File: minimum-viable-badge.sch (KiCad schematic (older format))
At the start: 33 parts, among them J1 EDGE_CONNECTOR, P1 BATTERY, P11 MECH, P12 MECH, P13 MECH, P2 USB, P3 BUTTON_A, P4 BUTTON_B, P6 POT_LONG, P9 POT_SHORT, Q1 S8050, Q2 S8050, SW1 PRGM, SW2 RESET, U1 CP2102, U2 ESP32-WROOM

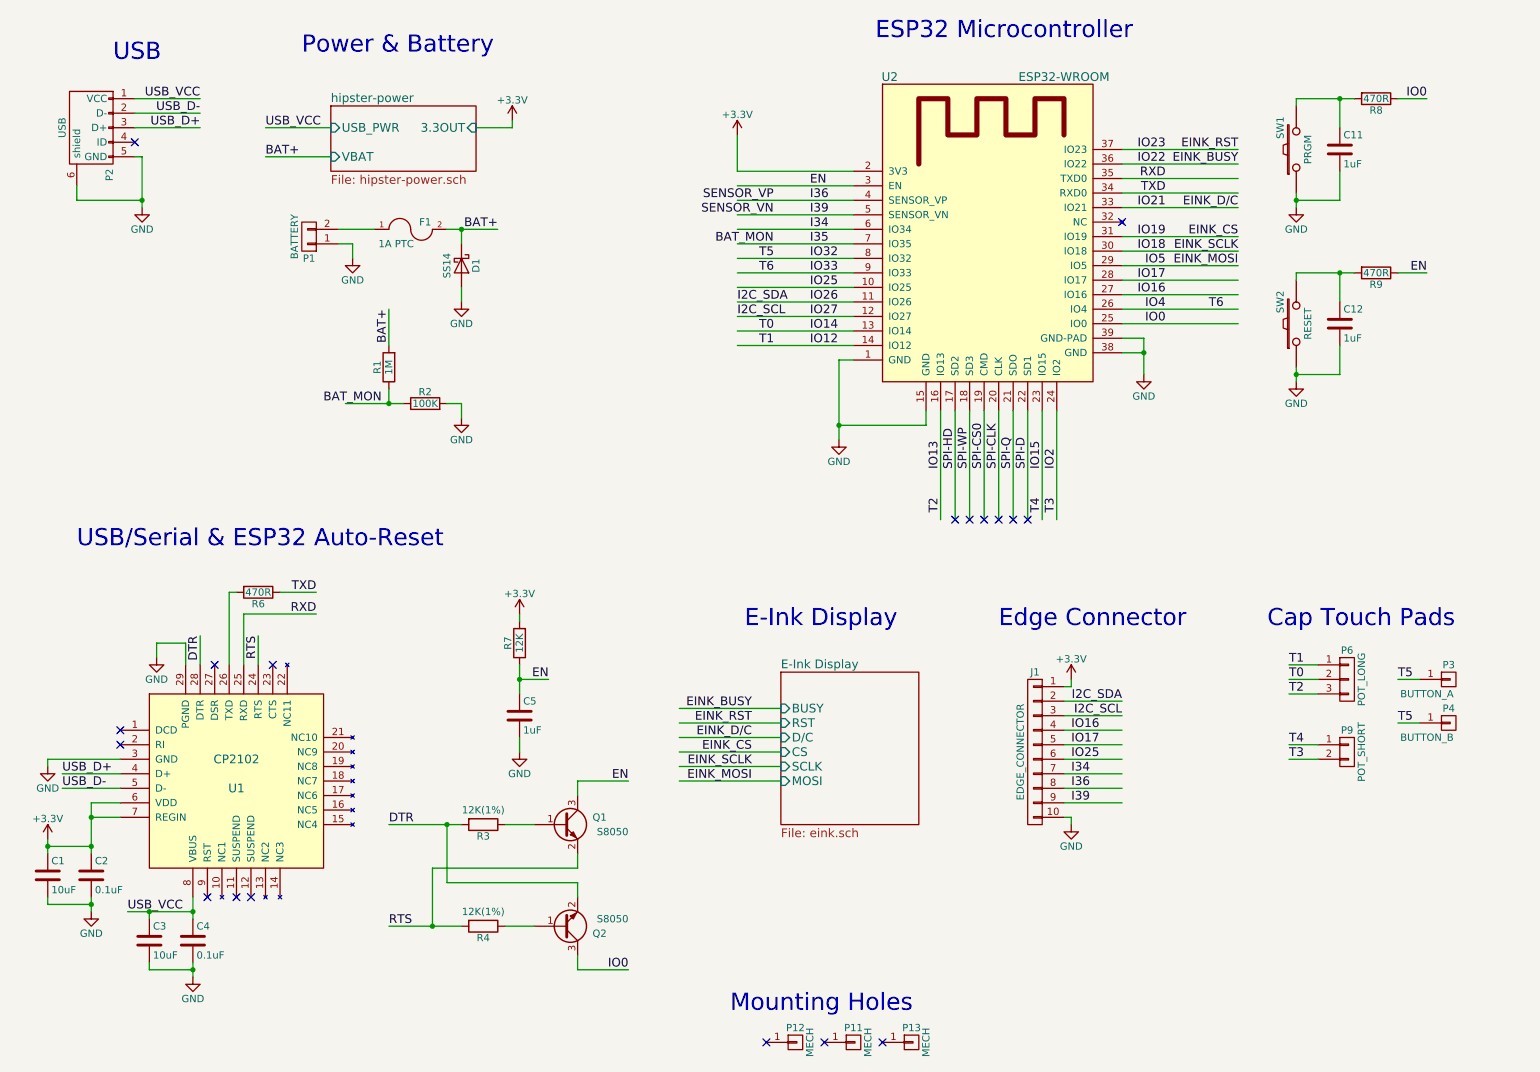
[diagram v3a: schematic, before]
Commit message: Add e-ink gate drive circuitry
Closes #14
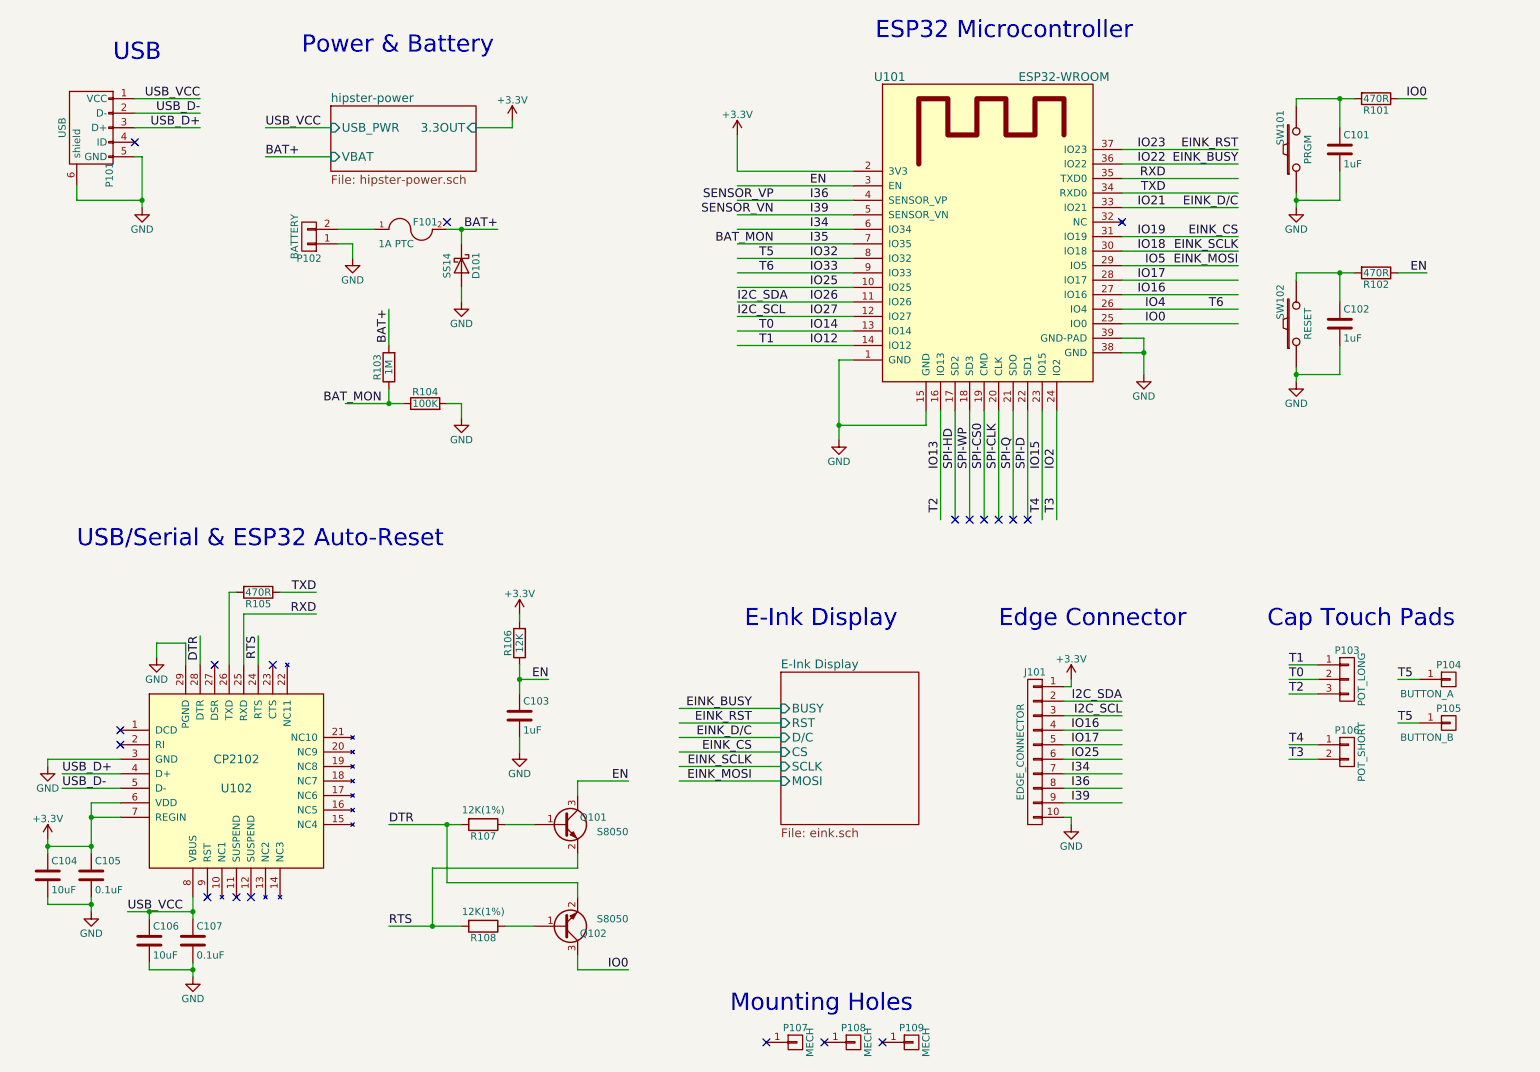
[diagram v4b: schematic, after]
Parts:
- renumbered C11 to C101, C12 to C102, C5 to C103, C1 to C104, C2 to C105, C3 to C106, C4 to C107, D1 to D101, F1 to F101, J1 to J101, P2 to P101, P1 to P102, P6 to P103, P3 to P104, P4 to P105, P9 to P106, P12 to P107, P11 to P108, P13 to P109, Q1 to Q101, Q2 to Q102, R8 to R101, R9 to R102, R1 to R103, R2 to R104, R6 to R105, R7 to R106, R3 to R107, R4 to R108, SW1 to SW101, SW2 to SW102, U2 to U101, U1 to U102
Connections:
- no-connect marks 18 -> 19
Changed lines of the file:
@@
 $EndDescr
 $Comp
-L ESP32-WROOM U2
+L ESP32-WROOM U101
 U 1 1 5919B2AF
 P 7350 2250
-F 0 "U2" H 6650 3500 60  0000 C CNN
+F 0 "U101" H 6650 3500 60  0000 C CNN
 F 1 "ESP32-WROOM" H 7850 3500 60  0000 C CNN
 F 2 "ESP32-footprints-Lib:ESP32-WROOM" H 7700 3600 60  0001 C CNN
@@
 EN
 $Comp
-L R R8
+L R R101
 U 1 1 59270A5B
 P 10000 1150
-F 0 "R8" V 10080 1150 50  0000 C CNN
+F 0 "R101" V 10080 1150 50  0000 C CNN
 F 1 "470R" V 10000 1150 50  0000 C CNN
 F 2 "Resistors_SMD:R_0603_HandSoldering" V 9930 1150 50  0001 C CNN
@@
 $EndComp
 $Comp
-L C C11
+L C C101
 U 1 1 59270B98
 P 9750 1500
-F 0 "C11" H 9775 1600 50  0000 L CNN
+F 0 "C101" H 9775 1600 50  0000 L CNN
 F 1 "1uF" H 9775 1400 50  0000 L CNN
 F 2 "Capacitors_SMD:C_0603_HandSoldering" H 9788 1350 50  0001 C CNN
@@
 $EndComp
 $Comp
-L SW_PUSH SW1
+L SW_PUSH SW101
 U 1 1 59270D01
 P 9450 1500
-F 0 "SW1" H 9600 1610 50  0000 C CNN
+F 0 "SW101" H 9600 1610 50  0000 C CNN
 F 1 "PRGM" H 9450 1420 50  0000 C CNN
 F 2 "Buttons_Switches_ThroughHole:SW_PUSH_SMALL" H 9450 1500 50  0001 C CNN
@@
 IO0
 $Comp
-L R R9
+L R R102
 U 1 1 59271D5C
 P 10000 2350
-F 0 "R9" V 10080 2350 50  0000 C CNN
+F 0 "R102" V 10080 2350 50  0000 C CNN
 F 1 "470R" V 10000 2350 50  0000 C CNN
 F 2 "Resistors_SMD:R_0603_HandSoldering" V 9930 2350 50  0001 C CNN
@@
 $EndComp
 $Comp
-L C C12
+L C C102
 U 1 1 59271D62
 P 9750 2700
-F 0 "C12" H 9775 2800 50  0000 L CNN
+F 0 "C102" H 9775 2800 50  0000 L CNN
 F 1 "1uF" H 9775 2600 50  0000 L CNN
 F 2 "Capacitors_SMD:C_0603_HandSoldering" H 9788 2550 50  0001 C CNN
@@
 $EndComp
 $Comp
-L SW_PUSH SW2
+L SW_PUSH SW102
 U 1 1 59271D68
 P 9450 2700
-F 0 "SW2" H 9600 2810 50  0000 C CNN
+F 0 "SW102" H 9600 2810 50  0000 C CNN
 F 1 "RESET" H 9450 2620 50  0000 C CNN
 F 2 "Buttons_Switches_ThroughHole:SW_PUSH_SMALL" H 9450 2700 50  0001 C CNN
@@
 EN
 $Comp
-L R R7
+L R R106
 U 1 1 59271E2F
 P 4100 4900
-F 0 "R7" V 4180 4900 50  0000 C CNN
+F 0 "R106" V 4180 4900 50  0000 C CNN
 F 1 "12K" V 4100 4900 50  0000 C CNN
 F 2 "Resistors_SMD:R_0603_HandSoldering" V 4030 4900 50  0001 C CNN
@@
 EN
 $Comp
-L USB_OTG-RESCUE-minimum-viable-badge P2
+L USB_OTG-RESCUE-minimum-viable-badge P101
 U 1 1 59272DBA
 P 1150 1350
-F 0 "P2" H 1475 1225 50  0000 C CNN
+F 0 "P101" H 1475 1225 50  0000 C CNN
 F 1 "USB" H 1150 1550 50  0000 C CNN
 F 2 "libs:USB-MICRO-5pin_PTHMOUNT-Amphenol.10118194-0001LF" V 1100 1250 50  0001 C CNN
@@
 USB_D+
 $Comp
-L CP2102 U1
+L CP2102 U102
 U 1 1 59276A0D
 P 2150 5850
-F 0 "U1" H 2150 5800 60  0000 C CNN
+F 0 "U102" H 2150 5800 60  0000 C CNN
 F 1 "CP2102" H 2150 6000 60  0000 C CNN
 F 2 "Housings_DFN_QFN:QFN-28-1EP_5x5mm_Pitch0.5mm" H 2150 5850 60  0001 C CNN
@@
 NoConn ~ 1950 6650
 $Comp
-L C C4
+L C C107
 U 1 1 59277F61
 P 1850 6950
-F 0 "C4" H 1875 7050 50  0000 L CNN
+F 0 "C107" H 1875 7050 50  0000 L CNN
 F 1 "0.1uF" H 1875 6850 50  0000 L CNN
 F 2 "Capacitors_SMD:C_0603_HandSoldering" H 1888 6800 50  0001 C CNN
@@
 $EndComp
 $Comp
-L C C3
+L C C106
 U 1 1 5927860D
 P 1550 6950
-F 0 "C3" H 1575 7050 50  0000 L CNN
+F 0 "C106" H 1575 7050 50  0000 L CNN
 F 1 "10uF" H 1575 6850 50  0000 L CNN
 F 2 "Capacitors_SMD:C_0805_HandSoldering" H 1588 6800 50  0001 C CNN
@@
 $EndComp
 $Comp
-L C C2
+L C C105
 U 1 1 59278B3D
 P 1150 6500
-F 0 "C2" H 1175 6600 50  0000 L CNN
+F 0 "C105" H 1175 6600 50  0000 L CNN
 F 1 "0.1uF" H 1175 6400 50  0000 L CNN
 F 2 "Capacitors_SMD:C_0603_HandSoldering" H 1188 6350 50  0001 C CNN
@@
 $EndComp
 $Comp
-L C C1
+L C C104
 U 1 1 59278B49
 P 850 6500
-F 0 "C1" H 875 6600 50  0000 L CNN
+F 0 "C104" H 875 6600 50  0000 L CNN
 F 1 "10uF" H 875 6400 50  0000 L CNN
 F 2 "Capacitors_SMD:C_0805_HandSoldering" H 888 6350 50  0001 C CNN
@@
 RXD
 $Comp
-L R R6
+L R R105
 U 1 1 5927B4F5
 P 2300 4550
-F 0 "R6" V 2380 4550 50  0000 C CNN
+F 0 "R105" V 2380 4550 50  0000 C CNN
 F 1 "470R" V 2300 4550 50  0000 C CNN
 F 2 "Resistors_SMD:R_0603_HandSoldering" V 2230 4550 50  0001 C CNN
@@
 $EndComp
 $Comp
-L R R4
+L R R108
 U 1 1 5927CC3C
 P 3850 6850
-F 0 "R4" V 3930 6850 50  0000 C CNN
+F 0 "R108" V 3930 6850 50  0000 C CNN
 F 1 "12K(1%)" V 3750 6850 50  0000 C CNN
 F 2 "Resistors_SMD:R_0603_HandSoldering" V 3780 6850 50  0001 C CNN
@@
 $EndComp
 $Comp
-L R R3
+L R R107
 U 1 1 5927D407
 P 3850 6150
-F 0 "R3" V 3930 6150 50  0000 C CNN
+F 0 "R107" V 3930 6150 50  0000 C CNN
 F 1 "12K(1%)" V 3750 6150 50  0000 C CNN
 F 2 "Resistors_SMD:R_0603_HandSoldering" V 3780 6150 50  0001 C CNN
@@
 RTS
 $Comp
-L R R1
+L R R103
 U 1 1 5927F23C
 P 3200 3000
-F 0 "R1" V 3280 3000 50  0000 C CNN
+F 0 "R103" V 3280 3000 50  0000 C CNN
 F 1 "1M" V 3200 3000 50  0000 C CNN
 F 2 "Resistors_SMD:R_0603_HandSoldering" V 3130 3000 50  0001 C CNN
@@
 $EndComp
 $Comp
-L R R2
+L R R104
 U 1 1 5927FA86
 P 3450 3250
-F 0 "R2" V 3530 3250 50  0000 C CNN
+F 0 "R104" V 3530 3250 50  0000 C CNN
 F 1 "100K" V 3450 3250 50  0000 C CNN
 F 2 "Resistors_SMD:R_0603_HandSoldering" V 3380 3250 50  0001 C CNN
@@
 BAT+
 $Comp
-L CONN_01X02 P1
+L CONN_01X02 P102
 U 1 1 592811CD
 P 2650 2100
-F 0 "P1" H 2650 2250 50  0000 C CNN
+F 0 "P102" H 2650 2250 50  0000 C CNN
 F 1 "BATTERY" V 2750 2100 50  0000 C CNN
 F 2 "Pin_Headers:Pin_Header_Angled_1x02_Pitch2.54mm" H 2650 2100 50  0001 C CNN
@@
 $EndComp
 $Comp
-L FUSE F1
+L FUSE F101
 U 1 1 59281797
 P 3350 2050
-F 0 "F1" H 3450 2100 50  0000 C CNN
+F 0 "F101" H 3450 2100 50  0000 C CNN
 F 1 "1A PTC" H 3250 1950 50  0000 C CNN
 F 2 "Diodes_SMD:D_1206" H 3350 2050 50  0001 C CNN
@@
 $EndComp
 $Comp
-L D_Schottky D1
+L D_Schottky D101
 U 1 1 59281A79
 P 3700 2300
-F 0 "D1" H 3700 2400 50  0000 C CNN
+F 0 "D101" H 3700 2400 50  0000 C CNN
 F 1 "SS14" H 3700 2200 50  0000 C CNN
 F 2 "Diodes_SMD:D_SMA" H 3700 2300 50  0001 C CNN
@@
 T1
 $Comp
-L CONN_01X02 P9
+L CONN_01X02 P106
 U 1 1 5937169B
 P 9800 5650
-F 0 "P9" H 9800 5800 50  0000 C CNN
+F 0 "P106" H 9800 5800 50  0000 C CNN
 F 1 "POT_SHORT" V 9900 5650 50  0000 C CNN
 F 2 "libs:sense_short" H 9800 5650 50  0001 C CNN
@@
 $EndComp
 $Comp
-L CONN_01X01 P13
+L CONN_01X01 P109
 U 1 1 5937F8C7
 P 6800 7650
-F 0 "P13" H 6800 7750 50  0000 C CNN
+F 0 "P109" H 6800 7750 50  0000 C CNN
 F 1 "MECH" V 6900 7650 50  0000 C CNN
 F 2 "Mounting_Holes:MountingHole_3.2mm_M3_Pad" H 6800 7650 50  0001 C CNN
@@
 $EndComp
 $Comp
-L CONN_01X01 P11
+L CONN_01X01 P108
 U 1 1 593802FC
 P 6400 7650
-F 0 "P11" H 6400 7750 50  0000 C CNN
+F 0 "P108" H 6400 7750 50  0000 C CNN
 F 1 "MECH" V 6500 7650 50  0000 C CNN
 F 2 "Mounting_Holes:MountingHole_3.2mm_M3_Pad" H 6400 7650 50  0001 C CNN
@@
 $EndComp
 $Comp
-L CONN_01X01 P12
+L CONN_01X01 P107
 U 1 1 593803BC
 P 6000 7650
-F 0 "P12" H 6000 7750 50  0000 C CNN
+F 0 "P107" H 6000 7750 50  0000 C CNN
 F 1 "MECH" V 6100 7650 50  0000 C CNN
 F 2 "Mounting_Holes:MountingHole_3.2mm_M3_Pad" H 6000 7650 50  0001 C CNN
@@
 $EndComp
 $Comp
-L Q_NPN_BEC Q1
+L Q_NPN_BEC Q101
 U 1 1 593FEB64
 P 4400 6150
-F 0 "Q1" H 4700 6200 50  0000 R CNN
+F 0 "Q101" H 4700 6200 50  0000 R CNN
 F 1 "S8050" H 4850 6100 50  0000 R CNN
 F 2 "TO_SOT_Packages_SMD:SOT-23_Handsoldering" H 4600 6250 50  0001 C CNN
@@
 $EndComp
 $Comp
-L Q_NPN_BEC Q2
+L Q_NPN_BEC Q102
 U 1 1 593FF3B5
 P 4400 6850
-F 0 "Q2" H 4700 6900 50  0000 R CNN
+F 0 "Q102" H 4700 6900 50  0000 R CNN
 F 1 "S8050" H 4850 6800 50  0000 R CNN
 F 2 "TO_SOT_Packages_SMD:SOT-23_Handsoldering" H 4600 6950 50  0001 C CNN
@@
 $EndComp
 $Comp
-L CONN_01X03 P6
+L CONN_01X03 P103
 U 1 1 59A0383A
 P 9800 5150
-F 0 "P6" H 9800 5350 50  0000 C CNN
+F 0 "P103" H 9800 5350 50  0000 C CNN
 F 1 "POT_LONG" V 9900 5150 50  0000 C CNN
 F 2 "libs:sense_long" H 9800 5150 50  0001 C CNN
@@
 	9400 5700 9600 5700
 $Comp
-L CONN_01X01 P3
+L CONN_01X01 P104
 U 1 1 59A413E1
 P 10500 5150
-F 0 "P3" H 10500 5250 50  0000 C CNN
+F 0 "P104" H 10500 5250 50  0000 C CNN
 F 1 "BUTTON_A" H 10350 5050 50  0000 C CNN
 F 2 "Mounting_Holes:MountingHole_3.2mm_M3_Pad" H 10500 5150 50  0001 C CNN
@@
 $EndComp
 $Comp
-L CONN_01X01 P4
+L CONN_01X01 P105
 U 1 1 59A41FB4
 P 10500 5450
-F 0 "P4" H 10500 5550 50  0000 C CNN
+F 0 "P105" H 10500 5550 50  0000 C CNN
 F 1 "BUTTON_B" H 10350 5350 50  0000 C CNN
 F 2 "Mounting_Holes:MountingHole_3.2mm_M3_Pad" H 10500 5450 50  0001 C CNN
@@
 	10300 5450 10150 5450
 $Comp
-L CONN_01X10 J1
+L CONN_01X10 J101
 U 1 1 59A46FD4
 P 7650 5650
-F 0 "J1" H 7650 6200 50  0000 C CNN
+F 0 "J101" H 7650 6200 50  0000 C CNN
 F 1 "EDGE_CONNECTOR" V 7750 5650 50  0000 C CNN
 F 2 "" H 7650 5650 50  0001 C CNN
@@
 $EndComp
 $Comp
-L C C5
+L C C103
 U 1 1 59A4FE66
 P 4100 5400
-F 0 "C5" H 4125 5500 50  0000 L CNN
+F 0 "C103" H 4125 5500 50  0000 L CNN
 F 1 "1uF" H 4125 5300 50  0000 L CNN
 F 2 "Capacitors_SMD:C_0603_HandSoldering" H 4138 5250 50  0001 C CNN
@@
 Wire Wire Line
 	1900 1150 1450 1150
+NoConn ~ 3600 2000
 $EndSCHEMATC
